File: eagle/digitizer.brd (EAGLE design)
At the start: 101.6 x 50.8 mm, 45 parts

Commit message: progress on digitizer layout
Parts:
- removed E$10, E$11, E$12: (no value), wirepad:1,6/0,8
- removed E$44: (no value), transistor:SOT223
- removed E$45: (no value), rcl:R0805
- removed E$63: (no value), ref-packages-longpad:PBGA256
- added C1, C2: 1n, rcl:R0805
- added C10, C11, C12, C13, C14, C15, C16, C17, C18, C19, C20, C21, C3, C4, C5, C6, C7, C8, C9, R4, R5, R6: (no value), rcl:R0805
- added C22, C23, C24, C25, C26, C27, R10, R11: (no value), rcl:R0402
- added D1, D2, R1, R7: 49.9, rcl:R0805
- added E$46: 240, rcl:R0402
- added J1, J2: (no value), Wurth_Elektronik_Passive_rev19e:7499811420
- added J5: (no value), SparkFun-Retired:SMA-EDGE
- added R2, R3: 33k, rcl:R0805
- added R8, R9: 330, rcl:R0805
- added U1, U2, U3: (no value), 74xx-us:TSSOP14
- added U4, U5: (no value), transistor:SOT223
- added U6: ADS4229, ref-packages-3d:QFN50P900X900X100-65T675
- added U7: (no value), ref-packages-longpad:PBGA256
- added U8, U9: (no value), ref-packages-3d:QFN50P700X700X100-49T470
- added X1: SIT3373AC-1E2-33NE250.000000X, SparkFun-Clocks:OSCILLATOR-SMD-7.5X5.2-6PIN
- E$1: device ref-packages-3d:QFN40P700X700X100-57T510 -> ref-packages:SOT23-5L
- E$13, E$14: value (none) -> 100n; device wirepad:1,6/0,8 -> rcl:R0402
- E$15: value (none) -> 100; device wirepad:1,6/0,8 -> rcl:R0402
- E$16: value (none) -> 240; device wirepad:1,6/0,8 -> rcl:R0402
- E$2: device ref-packages-3d:QFN50P900X900X100-65T675 -> ref-packages:SOT23-5L
- E$4: device Wurth_Elektronik_Electromechanic_Input-Output_Connectors_rev19d:692112030100 -> rcl:R0402
- E$9: device wirepad:1,6/0,8 -> rcl:R0402
- moved E$4 62.4 mm to (67.3, 29.8), turned to 0 degrees
- moved E$2 41.9 mm to (45.7, 3.17), turned to 0 degrees
- moved E$1 35.0 mm to (38.1, 3.17)
- moved E$14 29.9 mm to (86.4, 34.3)
- moved E$16 29.4 mm to (88.9, 35.6)
- moved E$13 28.8 mm to (86.4, 35.6)
- moved E$15 20.7 mm to (84.5, 34.9), turned to 90 degrees
- moved E$9 19.6 mm to (67.3, 40.0)
- renumbered E$5 to J3, E$6 to J4, E$7 to T1, E$8 to T2
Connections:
- new net !INV: U3.12, U3.8
- new net !PPS: R7.1, U2.1, U3.6
- new net ALIGN: R4.1, U2.6
- new net AMP1: C1.2, R2.2, U1.13
- new net AMP2: C2.1, R2.1, U1.12
- new net AMP3: C2.2, R3.2, U1.11
- new net BPSK: R3.1, U1.10, U2.5, U3.2
- new net DELAY: C13.2, R7.2, U1.5
- new net FB: C5.2, R6.2, X1.1
- new net FILT1: C3.2, R4.2, R5.1
- new net FILT2: C4.2, R5.2, R6.1
- new net IF1: J3.SIG, T1.6
- new net IF2: J4.SIG, T2.6
- new net INV: U2.12, U3.9
- new net LCLK: U2.3, U2.4
- new net OCLK: U2.11, U2.2, U3.3
- new net REF: C1.1, J5.SIG, R1.1
- new net S$1: E$13.1, E$15.2, U6.26
- new net S$19: E$14.1, E$15.1, U6.25
- new net S$20: E$13.2, E$16.1, X1.NC1
- new net S$22: J1.11, U8.1
- new net S$23: J1.10, U8.2
- new net S$24: C14.1, J1.6
- new net S$25: C15.1, J1.12
- new net S$26: C18.1, J1.1
- new net S$27: C16.1, J1.7
- new net S$28: C19.1, J2.6
- new net S$29: C17.1, J2.12
- new net S$30: C20.1, J2.1
- new net S$31: C21.1, J2.7
- new net S$32: J1.5, U8.5
- new net S$33: J1.4, U8.4
- new net S$34: J1.3, U8.7
- new net S$35: J1.2, U8.8
- new net S$36: J1.8, U8.10
- new net S$37: J1.9, U8.11
- new net S$38: J2.11, U9.1
- new net S$39: J2.10, U9.2
- new net S$40: J2.4, U9.4
- new net S$41: J2.5, U9.5
- new net S$42: J2.3, U9.7
- new net S$43: J2.2, U9.8
- new net S$44: J2.8, U9.10
- new net S$45: J2.9, U9.11
- new net S$46: R10.1, U8.12
- new net S$47: R11.1, U9.12
- new net TOGGLE: U1.6, U3.11
- new net V1.0: C23.1, C26.1, U8.24, U8.31, U8.42, U8.6, U9.24, U9.31, U9.42, U9.6
- new net V1.8: E$4.2, E$9.2, U6.1, U6.48, U8.19, U8.30, U8.41, U9.19, U9.30, U9.41
- new net V2.5: C22.1, C24.1, C25.1, C27.1, U8.3, U8.9, U9.3, U9.9
- net AVDD: now also C9.2, U5.3, U6.12, U6.16, U6.22, U6.33, U6.34; no longer E$2.12, E$2.16, E$2.22, E$2.33, E$2.34, E$44.3, E$45.2
- net GND: now also C10.1, C11.1, C12.1, C13.1, C14.2, C15.2, C16.2, C17.2, C18.2, C19.2, C20.2, C21.2, C22.2, C23.2, C24.2, C25.2, C26.2, C27.2, C3.1, C4.1, C5.1, C6.1, C7.1, C8.1, C9.1, D1.2, D2.2, E$16.2, E$4.1, E$46.2, J5.GND@0, J5.GND@1, J5.GND@2, J5.GND@3, R1.2, R10.2, R11.2, U1.1, U1.3, U1.7, U1.9, U2.10, U2.7, U2.9, U3.7, U4.2, U4.4, U5.2, U5.4, U6.13, U6.15, U6.17, U6.18, U6.21, U6.24, U6.27, U6.28, U6.31, U6.32, U6.35, U6.36, U6.37, U6.49, U6.65, U8.49, U9.49, X1.2, X1.NC0; no longer E$13.1, E$14.1, E$15.1, E$16.1, E$2.13, E$2.15, E$2.17, E$2.18, E$2.21, E$2.24, E$2.27, E$2.28, E$2.31, E$2.32, E$2.35, E$2.36, E$2.37, E$2.49, E$2.65, E$44.2, E$44.4, E$45.1
- net S$15: now also U6.30; no longer E$2.30
- net S$16: now also U6.29; no longer E$2.29
- net S$17: now also U6.20; no longer E$2.20
- net S$18: now also U6.19; no longer E$2.19
- net S$21: now also E$14.2, E$46.1, X1.3; no longer E$2.1, E$2.48
- net S$4: now also D1.1, R8.2; no longer J3.SIG, T1.6
- net S$5: now also D2.1, R9.2; no longer J4.SIG, T2.6
- net S$6: now also U6.23; no longer E$2.23
- net V3.3: now also C10.2, C11.2, C12.2, C6.2, C7.2, C8.2, U1.14, U2.14, U3.1, U3.10, U3.13, U3.14, U3.4, U4.3, U5.1, X1.4; no longer E$10.1, E$44.1
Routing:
- net BPSK: track 0.00 -> 37.8 mm, vias 0 -> 2
- net OCLK: track 0.00 -> 24.5 mm
- net AVDD: track 42.7 -> 20.2 mm
- net DELAY: track 0.00 -> 22.3 mm
- net !PPS: track 0.00 -> 22.0 mm
- net S$20: track 0.00 -> 16.6 mm, vias 0 -> 2
- net INV: track 0.00 -> 15.2 mm, vias 0 -> 2
- net S$21: track 0.00 -> 14.3 mm, vias 0 -> 2
- net FB: track 0.00 -> 12.4 mm
- net S$32: track 0.00 -> 10.4 mm, vias 0 -> 1
- net S$41: track 0.00 -> 10.4 mm, vias 0 -> 1
- net S$35: track 0.00 -> 10.2 mm
- net S$43: track 0.00 -> 10.2 mm
- net V1.8: track 0.00 -> 9.80 mm, vias 0 -> 8
- net V1.0: track 0.00 -> 9.75 mm, vias 0 -> 8
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- added copper zone on layer 15, net AVDD
- added copper zone on layer 2, net GND
- added copper zone on layer 16, net V1.0
- added copper zone on layer 15, net V1.8
- added copper zone on layer 15, net V2.5
- added copper zone on layer 1, net V3.3
- added copper zone on layer 15, net V3.3
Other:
- board text added: "ACTIVE"
- board text added: "PPS"

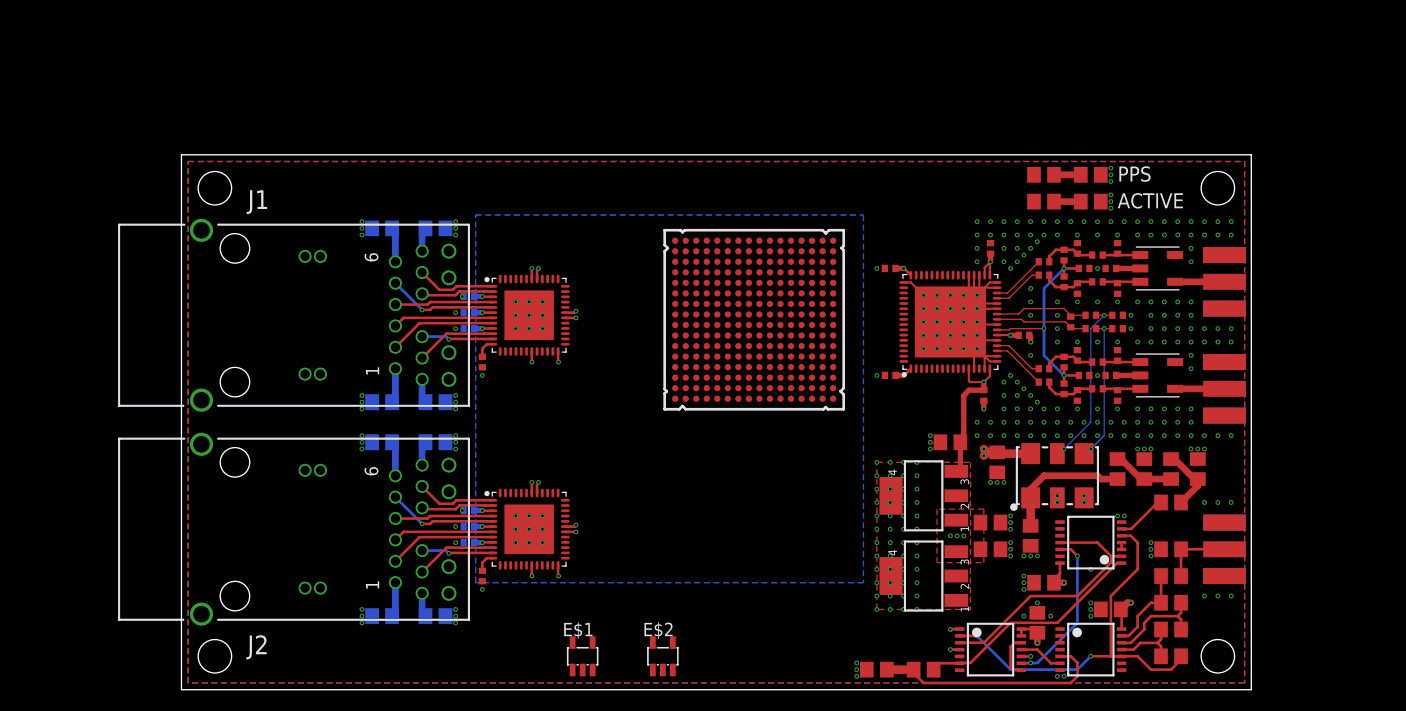
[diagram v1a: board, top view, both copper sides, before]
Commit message: add poe power supply simulation
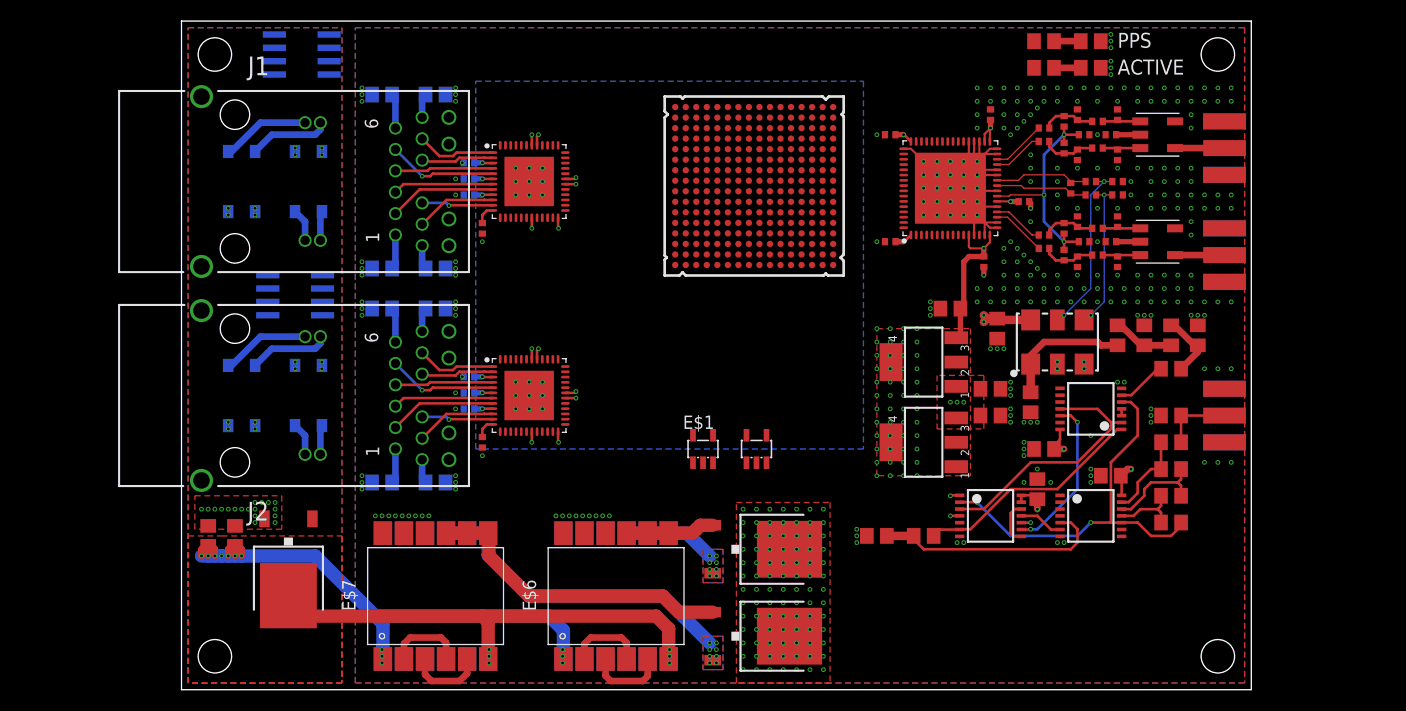
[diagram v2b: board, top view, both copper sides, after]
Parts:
- added C28, C29: (no value), rcl:R0805
- added D3, D4, D5, D6: MB1S, rectifier:TO-269AA
- added D7, D8: RBR10BM30AFH, transistor-fet:TO252
- added E$10, E$11, E$6, E$7: (no value), Wurth_Elektronik_Passive_rev19e:WE-POE_ER11/5
- added E$5, E$8: (no value), ref-packages:SOIC8
- added Q1: IPD530N15N3GATMA1, transistor-fet:TO252
- moved E$1 22.8 mm to (49.5, 22.9)
- moved E$2 21.6 mm to (54.6, 22.9)
- moved C14 12.7 mm to (19.1, 56.5)
- moved C15 12.7 mm to (24.1, 56.5)
- moved C16 12.7 mm to (24.1, 40.0)
- moved C18 12.7 mm to (19.1, 40.0)
- moved C23 12.7 mm to (27.3, 48.5)
- moved C24 12.7 mm to (27.3, 47.0)
- moved C3 12.7 mm to (96.5, 33.7)
- moved C4 12.7 mm to (91.4, 33.7)
- moved D2 12.7 mm to (86.4, 59.1)
- moved E$14 12.7 mm to (86.4, 47.0)
- moved E$15 12.7 mm to (84.5, 47.6)
- moved E$18 12.7 mm to (88.3, 42.5)
- moved E$19 12.7 mm to (88.9, 54.6)
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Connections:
- new net POE+: C28.1, C29.1, D3.+, D4.+, D5.+, D6.+, E$10.6, E$11.6, E$6.1, E$7.1
- new net POE-: C28.2, C29.2, D3.-, D4.-, D5.-, D6.-, Q1.2
- new net POE_SW: E$10.1, E$11.1, E$6.6, E$7.6, Q1.3
- new net RECT1: D7.1, E$6.7, E$6.8, E$6.9
- new net RECT2: D7.2, E$11.10, E$11.11, E$11.12
- new net RECT3: D8.1, E$7.7, E$7.8, E$7.9
- new net RECT4: D8.2, E$10.10, E$10.11, E$10.12
- new net S$48: D3.AC1, J1.14
- new net S$49: D3.AC2, J1.16
- new net S$50: D4.AC1, J1.15
- new net S$51: D4.AC2, J1.13
- new net S$52: D5.AC1, J2.14
- new net S$53: D5.AC2, J2.16
- new net S$54: D6.AC2, J2.13
- new net S$55: D6.AC1, J2.15
- new net S$56: E$7.2, E$7.4
- new net S$57: E$6.2, E$6.4
- new net S$58: E$7.3, E$7.5
- new net S$59: E$6.3, E$6.5
- new net V5: D7.3, D8.3
- net GND: now also E$10.7, E$10.8, E$10.9, E$11.7, E$11.8, E$11.9, E$6.10, E$6.11, E$6.12, E$7.10, E$7.11, E$7.12
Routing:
- net POE+: track 0.00 -> 58.2 mm, vias 0 -> 21
- net POE_SW: track 0.00 -> 48.7 mm, vias 0 -> 6
- net RECT4: track 0.00 -> 30.6 mm, vias 0 -> 8
- net RECT3: track 0.00 -> 29.6 mm
- net RECT2: track 0.00 -> 8.79 mm, vias 0 -> 8
- net RECT1: track 0.00 -> 8.48 mm
- net S$53: track 0.00 -> 8.44 mm
- net S$49: track 0.00 -> 8.44 mm
- net S$52: track 0.00 -> 7.72 mm
- net S$48: track 0.00 -> 7.72 mm
- net S$59: track 0.00 -> 7.62 mm
- net S$56: track 0.00 -> 7.44 mm
- net S$57: track 0.00 -> 7.44 mm
- net S$58: track 0.00 -> 7.40 mm
- net S$50: track 0.00 -> 3.13 mm
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- added copper zone on layer 15, net POE+
- added copper zone on layer 1, net POE-
- added copper zone on layer 16, net POE-
- added copper zone on layer 2, net POE-
- added copper zone on layer 1, net POE_SW
- added copper zone on layer 1, net RECT2
- added copper zone on layer 16, net RECT2
- added copper zone on layer 1, net RECT4
- added copper zone on layer 16, net RECT4
- added copper zone on layer 1, net V5
- added copper zone on layer 15, net V5
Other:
- board size 101.6 x 50.8 mm -> 101.6 x 63.5 mm

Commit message: progress on digitizer board
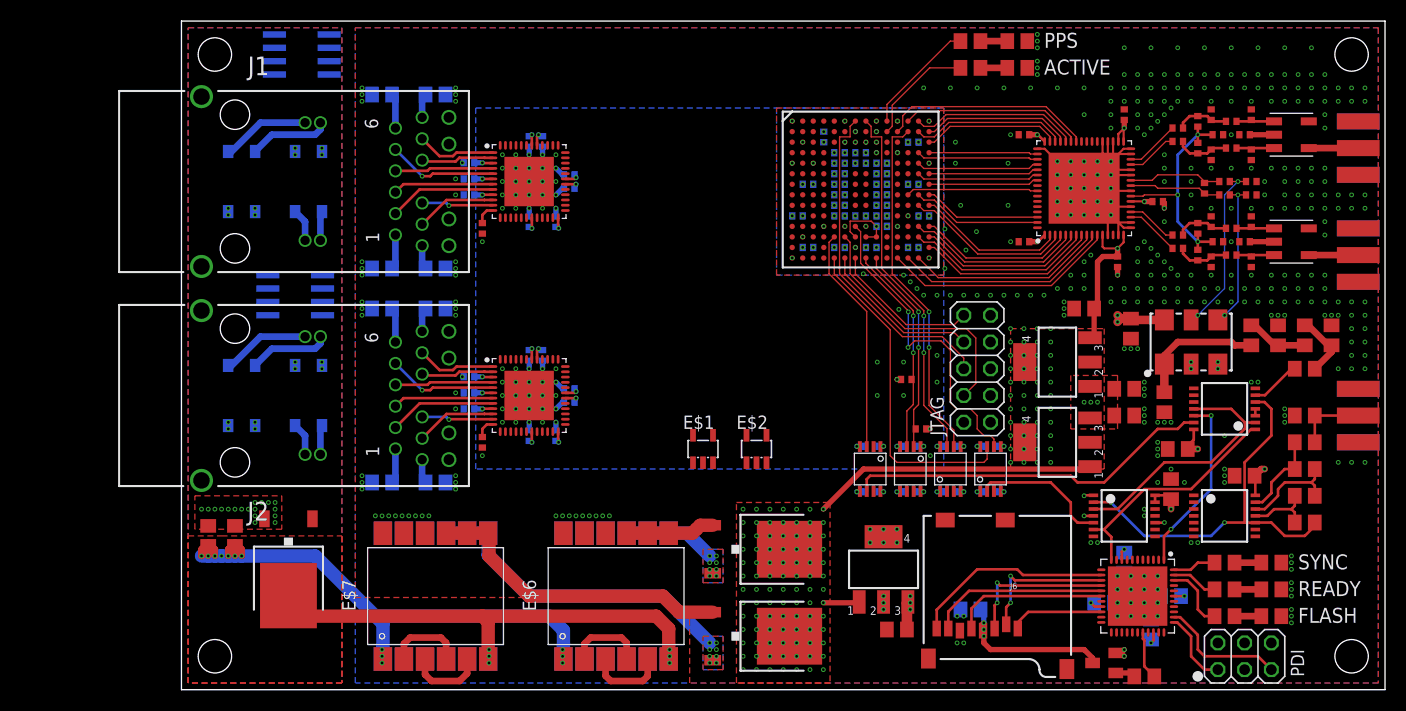
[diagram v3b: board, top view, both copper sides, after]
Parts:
- added C30, C58, C59, C60, C61: (no value), rcl:R0805
- added C31, C32, C33, C34, C35, C36, C37, C38, C39, C40, C41, C42, C43, C44, C45, C46, C47, C48, C49, C50, C51, C52, C53, C54, C55, C56, C57: 100n, rcl:R0402
- added C62, C63, C64, C65, C66, C67, C68, C69, C70, C71, C72, C73, C74, C75, C76, C77, C78, C79, C80, C81, C82, C83: (no value), rcl:R0402
- added D10, D11, D9: 49.9, rcl:R0805
- added E$12, E$3, E$44, E$45: (no value), on-semiconductor:MICRO8
- added J6: (no value), SparkFun-Connectors:MICRO-SD-SOCKET
- added JTAG: (no value), pinhead:2X05
- added PDI: (no value), pinhead:2X03
- added Q2: MMBT3906, ref-packages-longpad:SOT23-BEC
- added R12, R13: 330, rcl:R0805
- added R14: 2.2k, rcl:R0805
- added U10: (no value), transistor:SOT223
- added U11: (no value), ref-packages-3d:QFN50P700X700X100-45T565
- R7: value 49.9 -> 330
- U3: value (none) -> 74LVC74A
- U7: device ref-packages-longpad:PBGA256 -> custom:FTGB196
- moved R7 28.7 mm to (99.1, 12.1), turned to 0 degrees
- moved C1 12.7 mm to (106.7, 23.5)
- moved C11 12.7 mm to (101.0, 20.3)
- moved C12 12.7 mm to (94.0, 19.1)
- moved C2 12.7 mm to (106.7, 18.4)
- moved C3 12.7 mm to (109.2, 33.7)
- moved C4 12.7 mm to (104.1, 33.7)
- moved C5 12.7 mm to (93.3, 27.3)
- moved C6 12.7 mm to (90.2, 34.3)
- moved C7 12.7 mm to (89.5, 28.6)
- moved C8 12.7 mm to (89.5, 26.0)
- moved E$13 12.7 mm to (99.1, 48.3)
- moved E$14 12.7 mm to (99.1, 47.0)
- moved E$15 12.7 mm to (97.2, 47.6)
- moved E$17 12.7 mm to (101.0, 52.7)
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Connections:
- removed net !INV: U3.12, U3.8
- removed net DELAY: C13.2, R7.2, U1.5
- removed net TOGGLE: U1.6, U3.11
- new net !INIT: C82.2, E$3.3, U7.P8
- new net !PROGRAM: E$45.6, U7.L7
- new net !SCS: J6.CS, U11.14
- new net !SEN: R14.2, U11.29
- new net CCK: E$44.7, U7.A8
- new net CLK_25M: E$12.6, U2.13
- new net CLK_25M_A: E$12.3, U7.M5
- new net DA0: U6.42, U7.B11
- new net DA1: U6.43, U7.A12
- new net DA10: U6.54, U7.F13
- new net DA11: U6.55, U7.G14
- new net DA2: U6.44, U7.A13
- new net DA3: U6.45, U7.B14
- new net DA4: U6.46, U7.B13
- new net DA5: U6.47, U7.C14
- new net DA6: U6.50, U7.D14
- new net DA7: U6.51, U7.D13
- new net DA8: U6.52, U7.E13
- new net DA9: U6.53, U7.F14
- new net DB0: U6.62, U7.H14
- new net DB1: U6.63, U7.H13
- new net DB10: U6.10, U7.P12
- new net DB11: U6.11, U7.P11
- new net DB2: U6.2, U7.J14
- new net DB3: U6.3, U7.J13
- new net DB4: U6.4, U7.L14
- new net DB5: U6.5, U7.L13
- new net DB6: U6.6, U7.M14
- new net DB7: U6.7, U7.M13
- new net DB8: U6.8, U7.N14
- new net DB9: U6.9, U7.P13
- new net DCLK: U6.57, U7.H12
- new net DIN: E$44.6, U7.B12
- new net DONE: C83.1, E$3.2, U7.P9
- new net FPPS: E$45.7, U7.P5
- new net PDI_CLK: PDI.5, U11.35
- new net PDI_DAT: PDI.1, U11.34
- new net PPS: E$45.2, U3.5
- new net S$60: D9.1, R7.2
- new net S$61: D10.1, R12.2
- new net S$62: D11.1, R13.2
- new net S$63: R8.1, U7.A10
- new net S$64: Q2.B, R14.1
- new net S$65: R9.1, U7.B10
- new net S$66: U11.37
- new net S$67: R7.1, U11.44
- new net S$68: R12.1, U11.43
- new net S$69: R13.1, U11.42
- new net S$70: JTAG.4, U7.M6
- new net S$71: JTAG.8, U7.P6
- new net S$72: JTAG.10, U7.P7
- new net S$73: JTAG.6, U7.A7
- new net SCLK: J6.SCLK, U11.17
- new net SDI: J6.DI, U11.15
- new net SDO: J6.DO, U11.16
- new net SR1: J6.RSV2, U11.13
- new net SR2: J6.RSV1, U11.20
- new net V3.3D: C30.1, C58.2, C59.1, C60.2, C61.1, C77.1, C78.1, C79.2, C81.2, E$12.8, E$3.8, E$44.1, E$45.1, PDI.2, Q2.E, U10.3, U11.19, U11.31, U11.39, U11.9
- new net VSDC: C13.1, J6.VCC, Q2.C
- net !PPS: now also U11.11; no longer R7.1
- net GND: now also C13.2, C30.2, C31.2, C32.2, C33.2, C34.2, C35.2, C36.2, C37.2, C38.2, C39.2, C40.2, C41.2, C42.1, C43.1, C44.1, C45.1, C46.2, C47.2, C48.2, C49.1, C50.2, C51.1, C52.2, C53.2, C54.1, C55.1, C56.2, C57.2, C58.1, C59.2, C60.1, C61.2, C62.2, C63.2, C64.2, C65.2, C66.2, C67.2, C68.2, C69.2, C70.2, C71.2, C72.2, C73.2, C74.2, C75.2, C76.1, C77.2, C78.2, C79.1, C80.1, C81.1, D10.2, D11.2, D9.2, E$12.2, E$12.4, E$12.5, E$3.4, E$3.5, E$44.4, E$44.5, E$45.4, E$45.5, J6.CD1, J6.CD2, J6.GND, J6.GND1, J6.GND3, JTAG.1, JTAG.3, JTAG.5, JTAG.7, JTAG.9, PDI.6, U1.5, U10.2, U10.4, U11.18, U11.30, U11.38, U11.45, U11.8, U3.11, U3.12, U7.A1, U7.A11, U7.A14, U7.A6, U7.A9, U7.B4, U7.B7, U7.B9, U7.C13, U7.C2, U7.C6, U7.C7, U7.C8, U7.C9, U7.D11, U7.D5, U7.D7, U7.D9, U7.E1, U7.E10, U7.E14, U7.E3, U7.E6, U7.E8, U7.F5, U7.F9, U7.G10, U7.G12, U7.G3, U7.G6, U7.H5, U7.H9, U7.J10, U7.J6, U7.K1, U7.K14, U7.K5, U7.K7, U7.K9, U7.L10, U7.L11, U7.L4, U7.L6, U7.L8, U7.N12, U7.N3, U7.N5, U7.N7, U7.N9, U7.P1, U7.P14; no longer C13.1
- net INV: now also U11.1; no longer U3.9
- net V1.0: now also C43.2, C44.2, C45.2, C46.1, C47.1, C48.1, C49.2, C50.1, C51.2, C52.1, C53.1, C54.2, C55.2, C62.1, C64.1, C66.1, C69.1, C71.1, C73.1, U7.D6, U7.D8, U7.E5, U7.E7, U7.E9, U7.F6, U7.G5, U7.G9, U7.H6, U7.J5, U7.J9, U7.K6, U7.K8
- net V1.8: now also C31.1, C32.1, C33.1, C34.1, C35.1, C36.1, C37.1, C38.1, C39.1, C40.1, C41.1, C42.2, C56.1, C57.1, C63.1, C65.1, C67.1, C68.1, C70.1, C72.1, C74.1, C75.1, C76.2, C80.2, C82.1, C83.2, E$12.1, E$3.1, E$44.8, E$45.8, JTAG.2, U7.C12, U7.C4, U7.F10, U7.G13, U7.G2, U7.H10, U7.K10, U7.K12, U7.K13, U7.K2, U7.L9, U7.M2, U7.M7, U7.M8, U7.M9, U7.N13, U7.N2, U7.N6, U7.N8
- net V5: now also U10.1, U4.1
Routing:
- net CLK_25M: track 0.00 -> 35.0 mm
- net CCK: track 0.00 -> 34.7 mm, vias 0 -> 2
- net DIN: track 0.00 -> 33.6 mm, vias 0 -> 2
- net S$73: track 0.00 -> 31.8 mm
- net FPPS: track 0.00 -> 31.7 mm
- net V5: track 0.00 -> 30.4 mm
- net !PROGRAM: track 0.00 -> 30.2 mm, vias 0 -> 2
- net S$70: track 0.00 -> 24.1 mm
- net DB11: track 0.00 -> 22.3 mm
- net DELAY: track 22.3 -> 0.00 mm
- net CLK_25M_A: track 0.00 -> 21.6 mm
- net DB10: track 0.00 -> 20.5 mm
- net !INIT: track 0.00 -> 20.3 mm, vias 0 -> 2
- net DA0: track 0.00 -> 20.2 mm
- net DONE: track 0.00 -> 20.0 mm, vias 0 -> 2
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- added copper zone on layer 15, net V1.0
- added copper zone on layer 15, net V3.3D
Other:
- board size 101.6 x 63.5 mm -> 114.3 x 63.5 mm
- board text added: "FLASH"
- board text added: "READY"
- board text added: "SYNC"
